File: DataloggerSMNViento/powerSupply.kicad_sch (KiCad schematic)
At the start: 5 parts

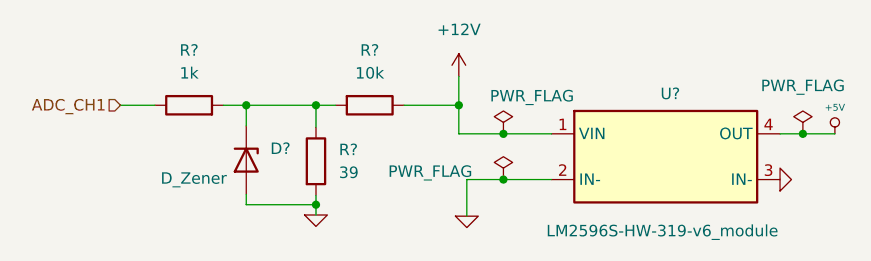
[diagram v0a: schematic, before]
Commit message: Agrego modificaciones al poncho de la EDU CIAA, también agrego una simulacion del circuito para tomar la tensión del ADC del tunnel
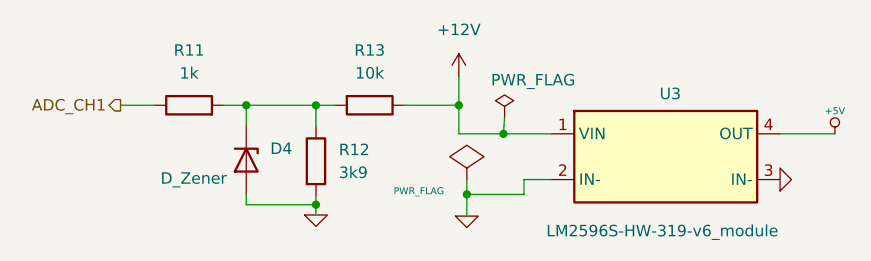
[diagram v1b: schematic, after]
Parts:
- D4: renamed from D?; footprint (none) -> Diode_THT:D_DO-35_SOD27_P12.70mm_Horizontal
- R11, R13: renamed from R?; footprint (none) -> Resistor_THT:R_Axial_DIN0207_L6.3mm_D2.5mm_P15.24mm_Horizontal
- R12: renamed from R?; value 39 -> 3k9; footprint (none) -> Resistor_THT:R_Axial_DIN0207_L6.3mm_D2.5mm_P15.24mm_Horizontal
- gave numbers to parts that had none: 1
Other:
- company: (none) -> Servicio Meteorológico Nacional - FIUBA - UBA
- title: (none) -> Datalogger para SCTV
